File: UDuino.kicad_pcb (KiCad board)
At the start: 2 copper layers, 27 parts, among them J1 Screw_Terminal_01x04, U1 NAU8315YG, U2 DRV8833RTY, U3 NAU8315YG, U4 STM32L452VCTx

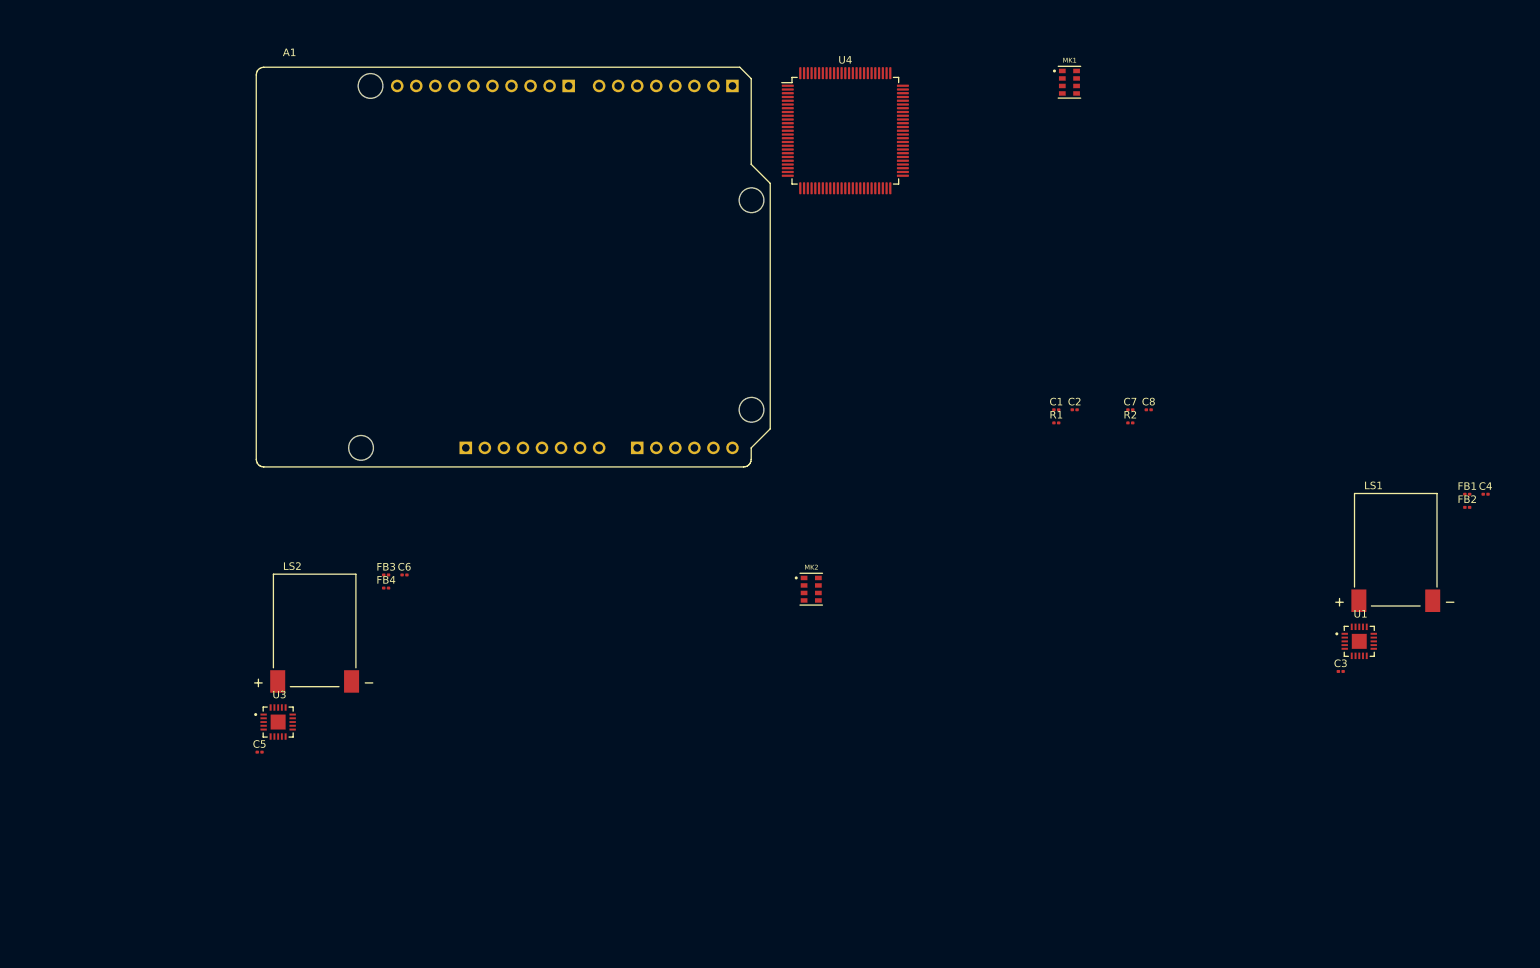
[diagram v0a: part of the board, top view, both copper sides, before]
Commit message: Rough placement of Speakers on board
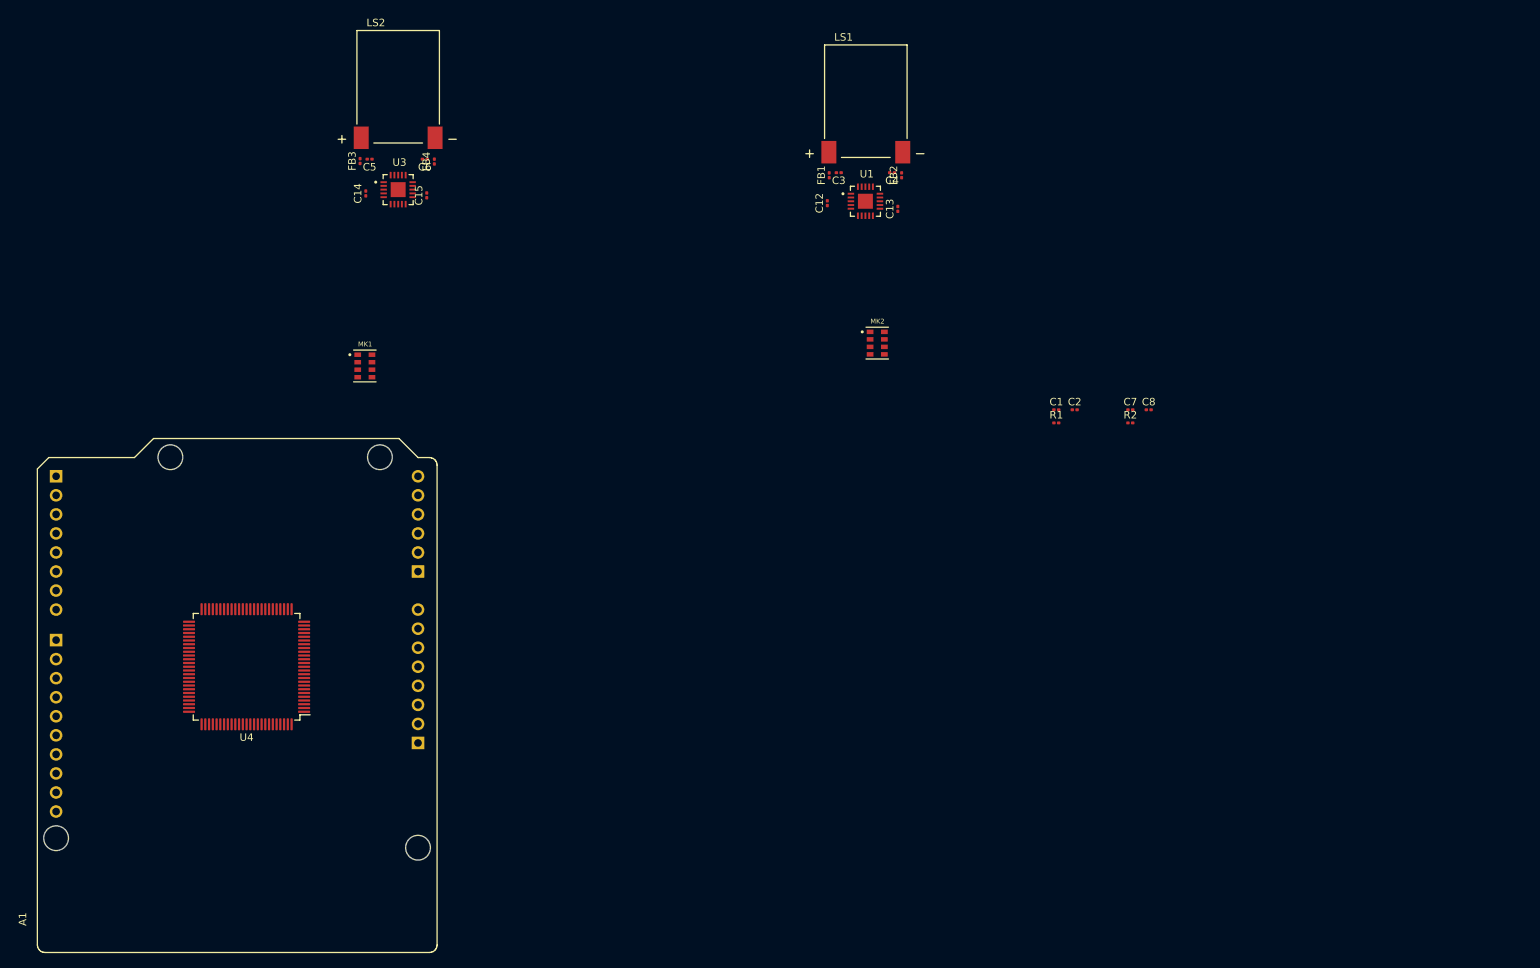
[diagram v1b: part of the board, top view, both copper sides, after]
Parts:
- added C12: 4u7, Capacitor_SMD:C_0201_0603Metric, F.Cu at (134.6, 56.3)
- added C13: 0u1, Capacitor_SMD:C_0201_0603Metric, F.Cu at (144.0, 57.0)
- added C14: 4u7, Capacitor_SMD:C_0201_0603Metric, F.Cu at (73.0, 55.0)
- added C15: 0u1, Capacitor_SMD:C_0201_0603Metric, F.Cu at (81.2, 55.2)
- moved U4 107.2 mm to (57.1, 118.1), turned to 180 degrees
- moved MK1 101.3 mm to (72.9, 78.0)
- moved FB1 95.1 mm to (134.8, 52.5), turned to 90 degrees
- moved C3 94.4 mm to (136.1, 52.2), turned to 180 degrees
- moved LS1 92.6 mm to (139.7, 42.7)
- moved C4 90.0 mm to (143.2, 52.2), turned to 180 degrees
- moved U1 88.2 mm to (139.6, 56.0)
- moved FB2 87.5 mm to (144.5, 52.5), turned to 90 degrees
- moved C5 80.4 mm to (73.5, 50.4), turned to 180 degrees
- moved LS2 73.3 mm to (77.3, 40.7)
- moved U3 72.8 mm to (77.3, 54.5)
- moved A1 69.1 mm to (82.5, 156.2), turned to 90 degrees
- moved FB4 57.2 mm to (82.2, 50.7), turned to 90 degrees
- moved C6 55.5 mm to (80.9, 50.4), turned to 180 degrees
- moved FB3 55.3 mm to (72.3, 50.7), turned to 90 degrees
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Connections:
- A1 pad D0: Net-(A1-PadD0) -> /UART4_RX
- A1 pad D1: Net-(A1-PadD1) -> /UART4_TX
- A1 pad D6: Net-(A1-PadD6) -> Net-(U4-Pad45)
- A1 pad D7: Net-(A1-PadD7) -> Net-(U4-Pad46)
- U4 pad 23: unconnected-(U4-Pad23) -> /UART4_TX
- U4 pad 24: unconnected-(U4-Pad24) -> /UART4_RX
- U4 pad 41: unconnected-(U4-Pad41) -> Net-(A1-PadD2)
- U4 pad 42: unconnected-(U4-Pad42) -> Net-(A1-PadD3)
- U4 pad 43: unconnected-(U4-Pad43) -> Net-(A1-PadD4)
- U4 pad 44: unconnected-(U4-Pad44) -> Net-(A1-PadD5)
- U4 pad 45: unconnected-(U4-Pad45) -> Net-(U4-Pad45)
- U4 pad 46: unconnected-(U4-Pad46) -> Net-(U4-Pad46)
- U4 pad 81: Net-(A1-PadD0) -> unconnected-(U4-Pad81)
- U4 pad 82: Net-(A1-PadD1) -> unconnected-(U4-Pad82)
- U4 pad 83: Net-(A1-PadD2) -> unconnected-(U4-Pad83)
- U4 pad 84: Net-(A1-PadD3) -> unconnected-(U4-Pad84)
- U4 pad 85: Net-(A1-PadD4) -> unconnected-(U4-Pad85)
- U4 pad 86: Net-(A1-PadD5) -> unconnected-(U4-Pad86)
- U4 pad 87: Net-(A1-PadD6) -> unconnected-(U4-Pad87)
- U4 pad 88: Net-(A1-PadD7) -> unconnected-(U4-Pad88)
- U4 pad 89: unconnected-(U4-Pad89) -> /SPI3_SCK
- U4 pad 90: unconnected-(U4-Pad90) -> /SPI3_MISO
- U4 pad 91: unconnected-(U4-Pad91) -> /SPI3_MOSI

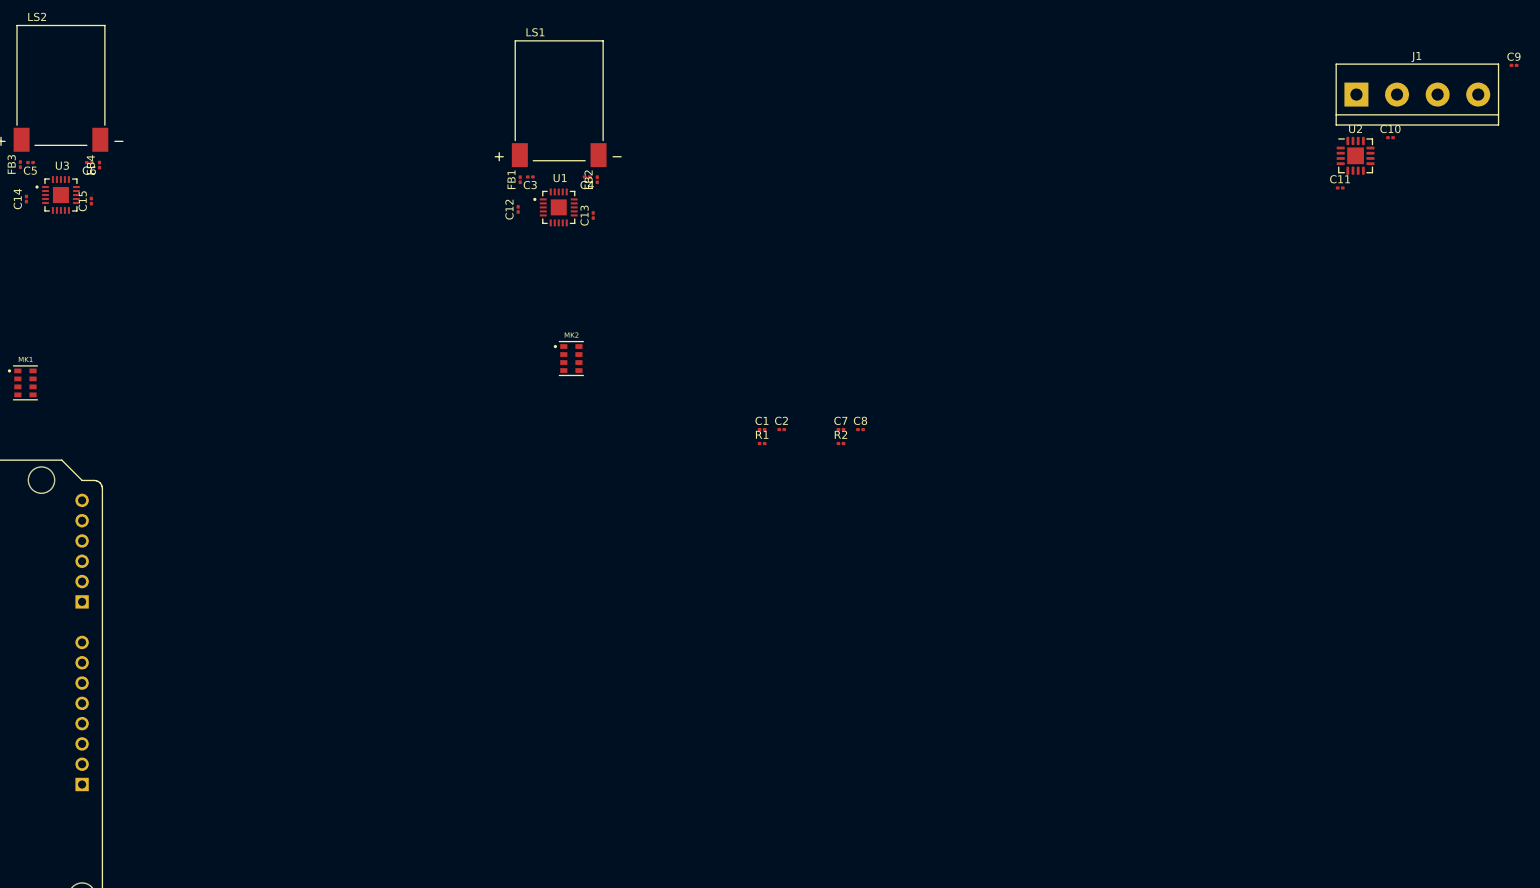
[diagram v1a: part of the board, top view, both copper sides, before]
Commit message: Rough placement of the Motor controller
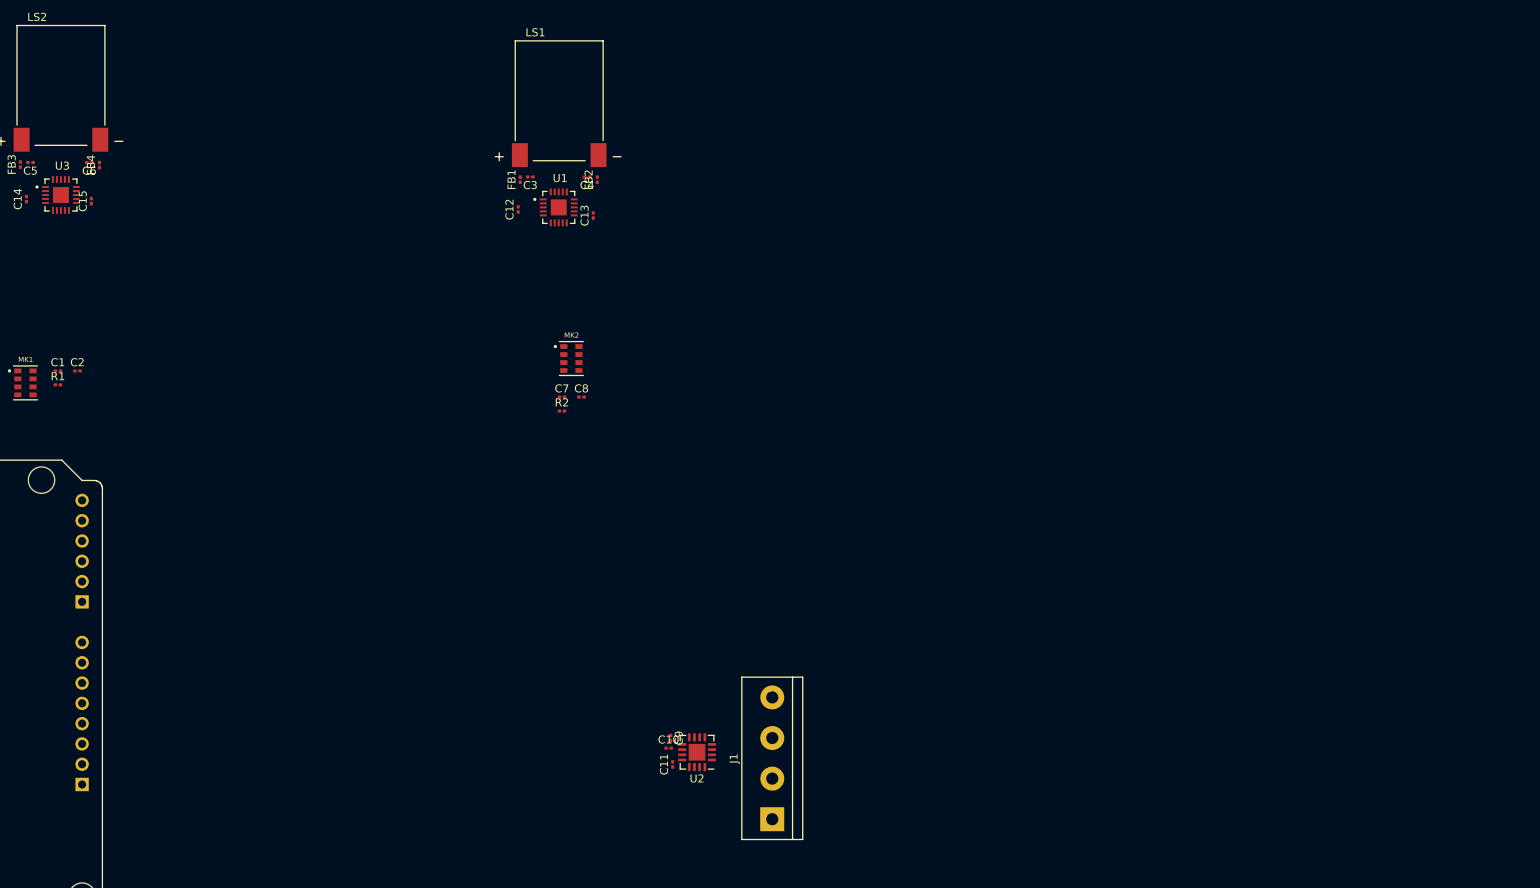
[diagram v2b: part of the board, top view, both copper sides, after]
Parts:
- moved C9 135.0 mm to (153.7, 122.4), turned to -90 degrees
- moved C10 118.3 mm to (153.4, 123.7)
- moved J1 116.5 mm to (166.4, 132.6), turned to 90 degrees
- moved U2 111.2 mm to (157.0, 124.2), turned to 180 degrees
- moved C11 110.4 mm to (153.9, 125.7), turned to 90 degrees
- moved C2 88.4 mm to (79.4, 76.5)
- moved C1 88.4 mm to (77.0, 76.5)
- moved R1 88.4 mm to (77.0, 78.2)
- moved C7 35.2 mm to (140.0, 79.8)
- moved C8 35.2 mm to (142.5, 79.8)
- moved R2 35.2 mm to (140.0, 81.5)
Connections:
- U4 pad 15: unconnected-(U4-Pad15) -> /Motor/AIN1
- U4 pad 16: unconnected-(U4-Pad16) -> /Motor/AIN2
- U4 pad 17: unconnected-(U4-Pad17) -> /Motor/BIN2
- U4 pad 18: unconnected-(U4-Pad18) -> /Motor/BIN1
